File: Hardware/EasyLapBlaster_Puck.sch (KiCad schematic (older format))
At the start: 34 parts, among them IC1 PIC10F322, P1 CONN_01X02, P2 CONN_01X06, Q1 AO3401A, Q2 AO3400A, SW1 SPST, U1 HS0038B, U2 DW-01, U3 FS8205

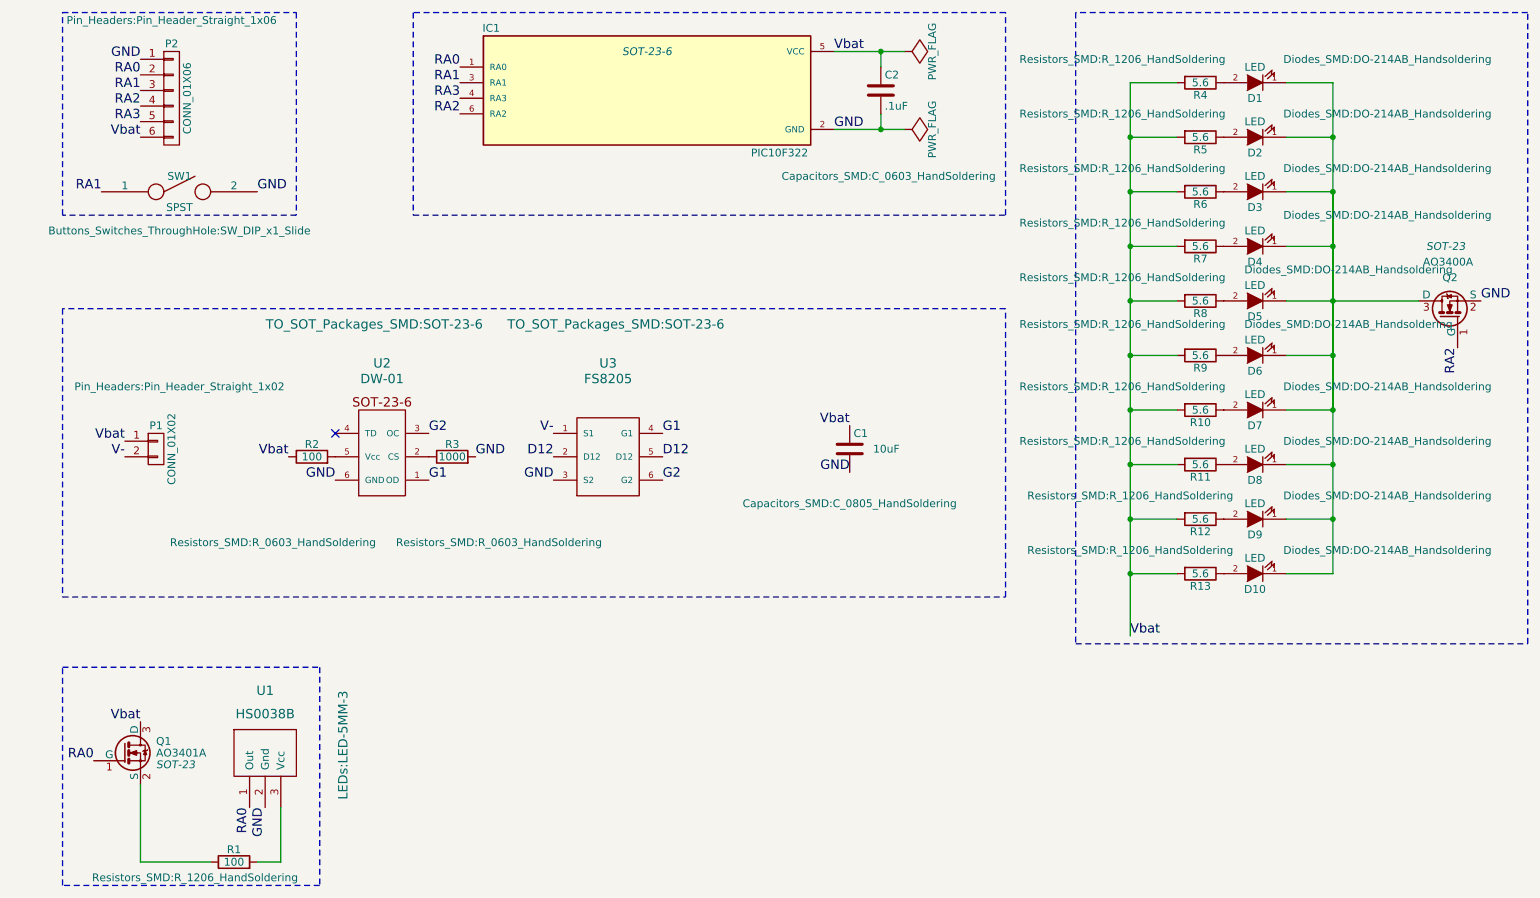
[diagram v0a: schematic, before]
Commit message: added LED footprint, rearranged led/resistor order for better heatsinking (VCC can be poured on the top layer)
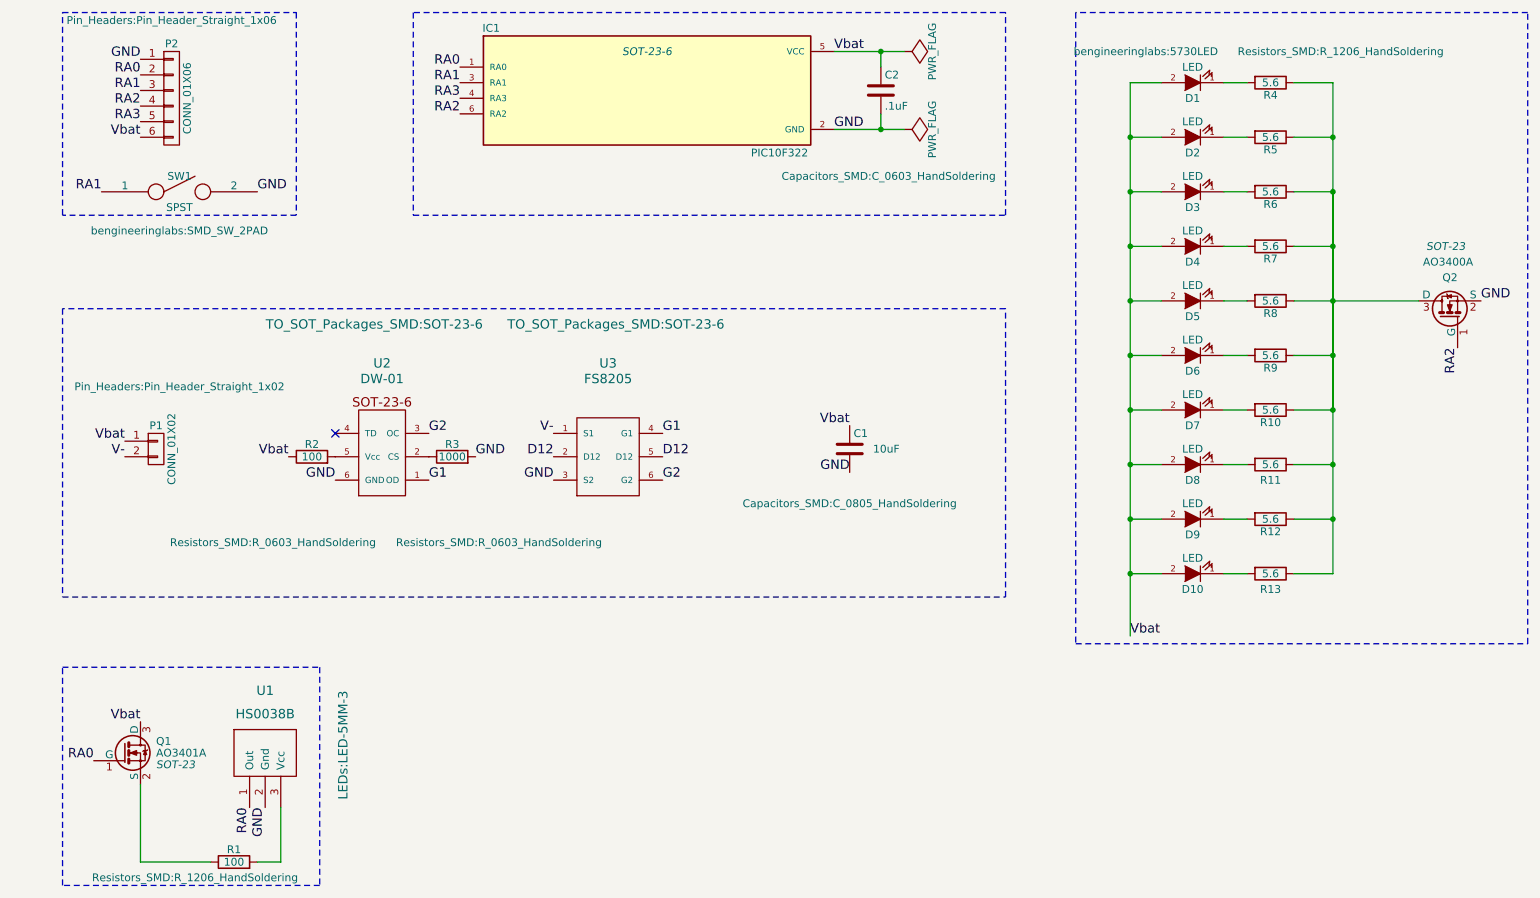
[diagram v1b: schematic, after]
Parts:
- D1, D10, D2, D3, D4, D5, D6, D7, D8, D9: footprint Diodes_SMD:DO-214AB_Handsoldering -> bengineeringlabs:5730LED
- SW1: footprint Buttons_Switches_ThroughHole:SW_DIP_x1_Slide -> bengineeringlabs:SMD_SW_2PAD
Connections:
- net Vbat: now also D1.2 (A), D10.2 (A), D2.2 (A), D3.2 (A), D4.2 (A), D5.2 (A), D6.2 (A), D7.2 (A), D8.2 (A), D9.2 (A); no longer R10.2, R11.2, R12.2, R13.2, R4.2, R5.2, R6.2, R7.2, R8.2, R9.2
- net at R7.1: now also Q2.3 (D), R10.1, R11.1, R12.1, R13.1, R4.1, R5.1, R6.1, R8.1, R9.1; no longer D4.2 (A)
- new net: D4.1 (K), R7.2
- new net: D5.1 (K), R8.2
- new net: D6.1 (K), R9.2
- new net: D1.1 (K), R4.2
- new net: D2.1 (K), R5.2
- new net: D3.1 (K), R6.2
- new net: D7.1 (K), R10.2
- new net: D8.1 (K), R11.2
- new net: D9.1 (K), R12.2
- new net: D10.1 (K), R13.2
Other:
- moved on the sheet: D1, D10, D2, D3, D4, D5, D6, D7, D8, D9, R10, R11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

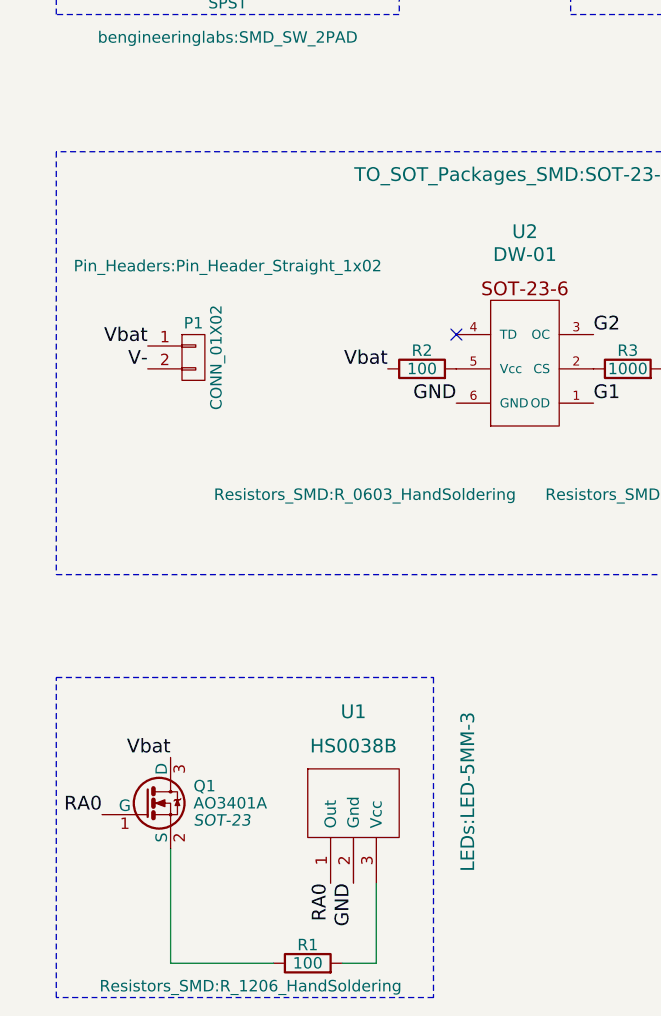
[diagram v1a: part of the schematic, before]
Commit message: added 18650 footprint, added to schematic
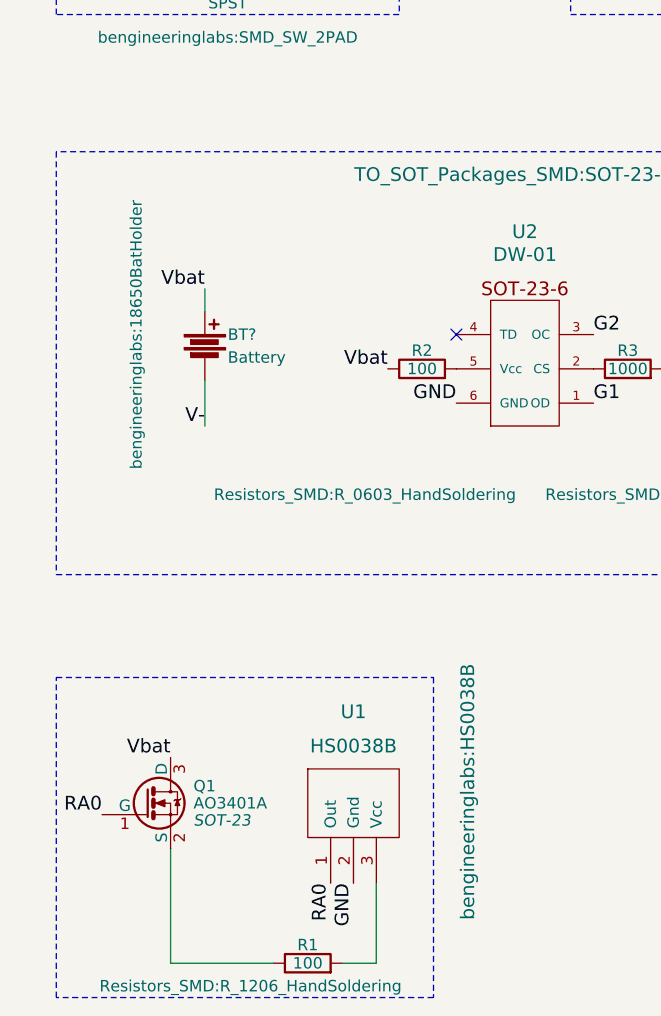
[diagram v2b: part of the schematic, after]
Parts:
- removed P1: CONN_01X02, Pin_Headers:Pin_Header_Straight_1x02, symbol CONN_01X02
- added BT?: Battery, bengineeringlabs:18650BatHolder, symbol Battery
- U1: footprint LEDs:LED-5MM-3 -> bengineeringlabs:HS0038B
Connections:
- net V-: now also BT?.2
- net Vbat: now also BT?.1
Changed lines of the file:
@@
 Text Label 1650 2100 2    60   ~ 0
 RA2
-$Comp
-L CONN_01X02 P1
-U 1 1 5746AD50
-P 1750 4300
-F 0 "P1" H 1750 4450 50  0000 C CNN
-F 1 "CONN_01X02" V 1850 4300 50  0000 C CNN
-F 2 "Pin_Headers:Pin_Header_Straight_1x02" H 1900 4700 50  0000 C CNN
-F 3 "" H 1750 4300 50  0000 C CNN
-	1    1750 4300
-	1    0    0    -1
-$EndComp
-Text Label 1550 4250 2    60   ~ 0
+Text Label 1800 4000 2    60   ~ 0
 Vbat
-Text Label 1550 4350 2    60   ~ 0
+Text Label 1800 4600 2    60   ~ 0
 V-
 $Comp
@@
 F 0 "U1" H 2450 6750 60  0000 C CNN
 F 1 "HS0038B" H 2450 6600 60  0000 C CNN
-F 2 "LEDs:LED-5MM-3" V 2950 6400 60  0000 C CNN
+F 2 "bengineeringlabs:HS0038B" V 2950 6400 60  0000 C CNN
 F 3 "" H 2400 6350 60  0000 C CNN
 	1    2450 6300
@@
 Wire Wire Line
 	9300 5100 9050 5100
+$Comp
+L Battery BT?
+U 1 1 5763802F
+P 1800 4250
+F 0 "BT?" H 1900 4300 50  0000 L CNN
+F 1 "Battery" H 1900 4200 50  0000 L CNN
+F 2 "bengineeringlabs:18650BatHolder" V 1500 4300 50  0000 C CNN
+F 3 "" V 1800 4290 50  0000 C CNN
+	1    1800 4250
+	1    0    0    -1
+$EndComp
+Wire Wire Line
+	1800 4400 1800 4600
+Wire Wire Line
+	1800 4000 1800 4100
 $EndSCHEMATC

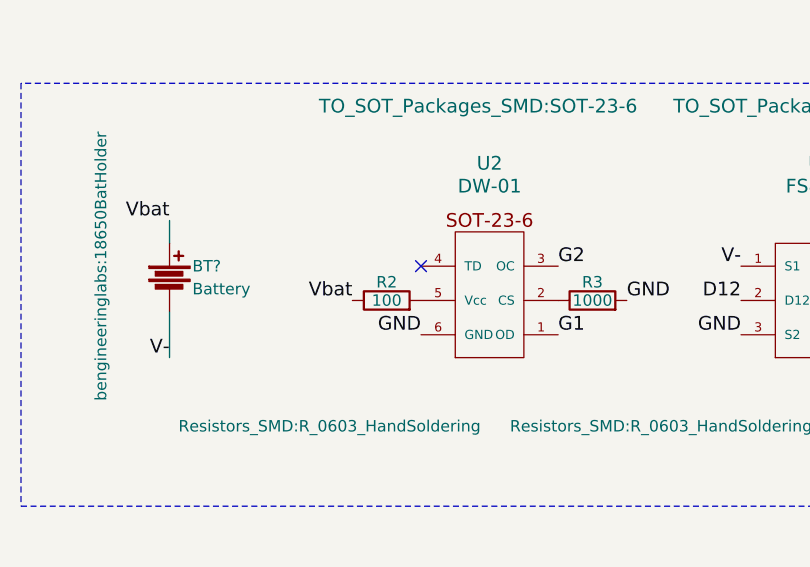
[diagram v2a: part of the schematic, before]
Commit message: netlist updated on board file, layout is still a mess
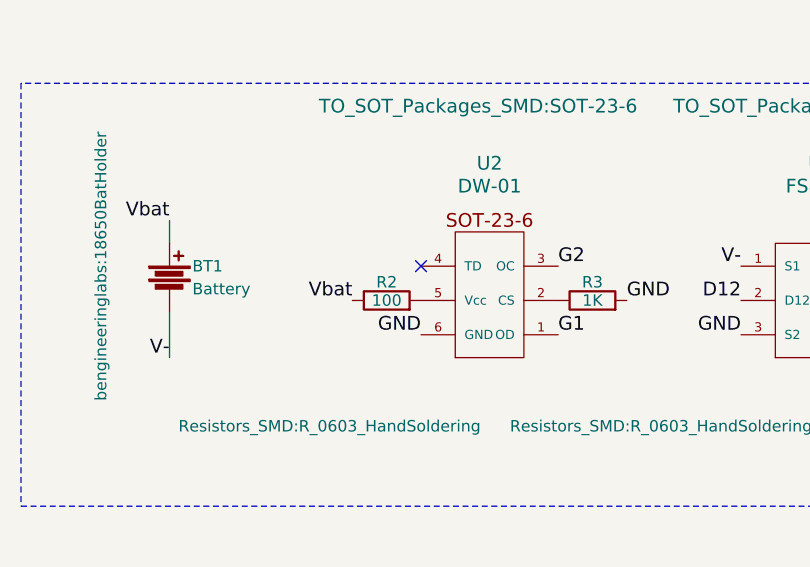
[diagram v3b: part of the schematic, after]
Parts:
- R3: value 1000 -> 1K
- gave numbers to parts that had none: 1
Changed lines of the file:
@@
 RA2
 $Comp
-L PWR_FLAG #FLG01
+L PWR_FLAG #FLG1
 U 1 1 57469CB9
 P 6550 1750
-F 0 "#FLG01" H 6550 1845 50  0001 C CNN
+F 0 "#FLG1" H 6550 1845 50  0001 C CNN
 F 1 "PWR_FLAG" H 6550 1930 50  0000 C CNN
 F 2 "" H 6550 1750 50  0000 C CNN
@@
 $EndComp
 $Comp
-L PWR_FLAG #FLG02
+L PWR_FLAG #FLG2
 U 1 1 57469CE5
 P 6550 2250
-F 0 "#FLG02" H 6550 2345 50  0001 C CNN
+F 0 "#FLG2" H 6550 2345 50  0001 C CNN
 F 1 "PWR_FLAG" H 6550 2430 50  0000 C CNN
 F 2 "" H 6550 2250 50  0000 C CNN
@@
 P 3650 4350
 F 0 "R3" V 3730 4350 50  0000 C CNN
-F 1 "1000" V 3650 4350 50  0000 C CNN
+F 1 "1K" V 3650 4350 50  0000 C CNN
 F 2 "Resistors_SMD:R_0603_HandSoldering" V 3100 4050 50  0000 C CNN
 F 3 "" H 3650 4350 50  0000 C CNN
@@
 	9300 5100 9050 5100
 $Comp
-L Battery BT?
+L Battery BT1
 U 1 1 5763802F
 P 1800 4250
-F 0 "BT?" H 1900 4300 50  0000 L CNN
+F 0 "BT1" H 1900 4300 50  0000 L CNN
 F 1 "Battery" H 1900 4200 50  0000 L CNN
 F 2 "bengineeringlabs:18650BatHolder" V 1500 4300 50  0000 C CNN
